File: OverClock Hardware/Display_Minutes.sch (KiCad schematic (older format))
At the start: 40 parts, among them U3 10M02SCE144

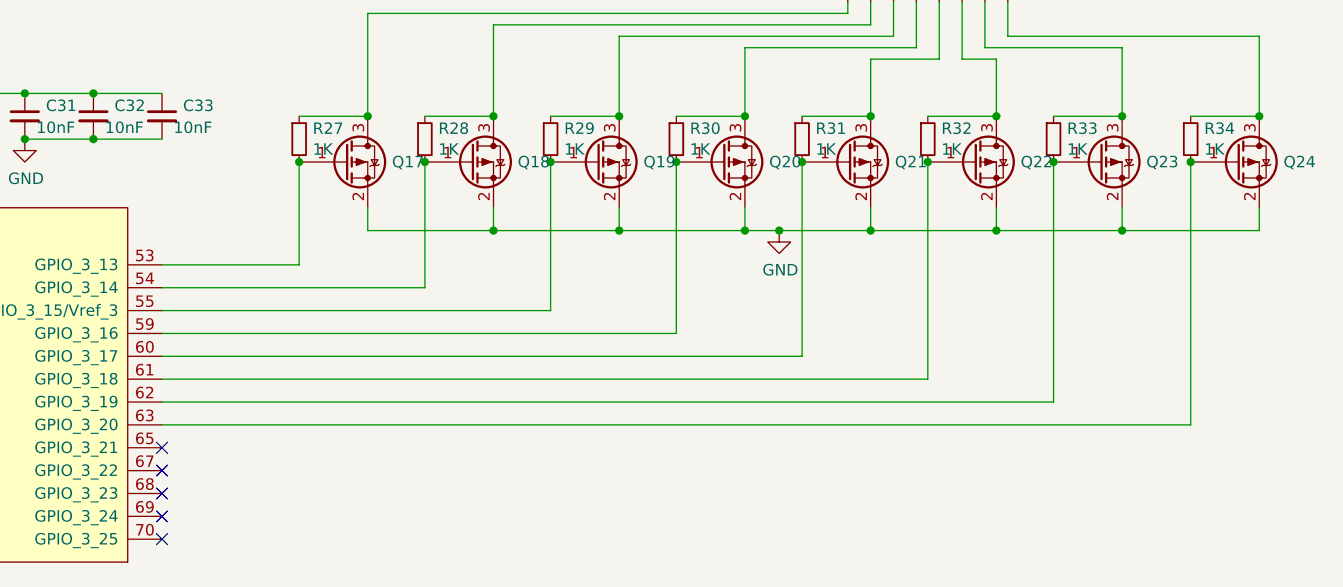
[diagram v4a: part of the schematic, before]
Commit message: Rerouted 7 Segment Displays
Rearranged the displays for cleaner routing, also modified the schematic for some of the displays to allow for better routing.
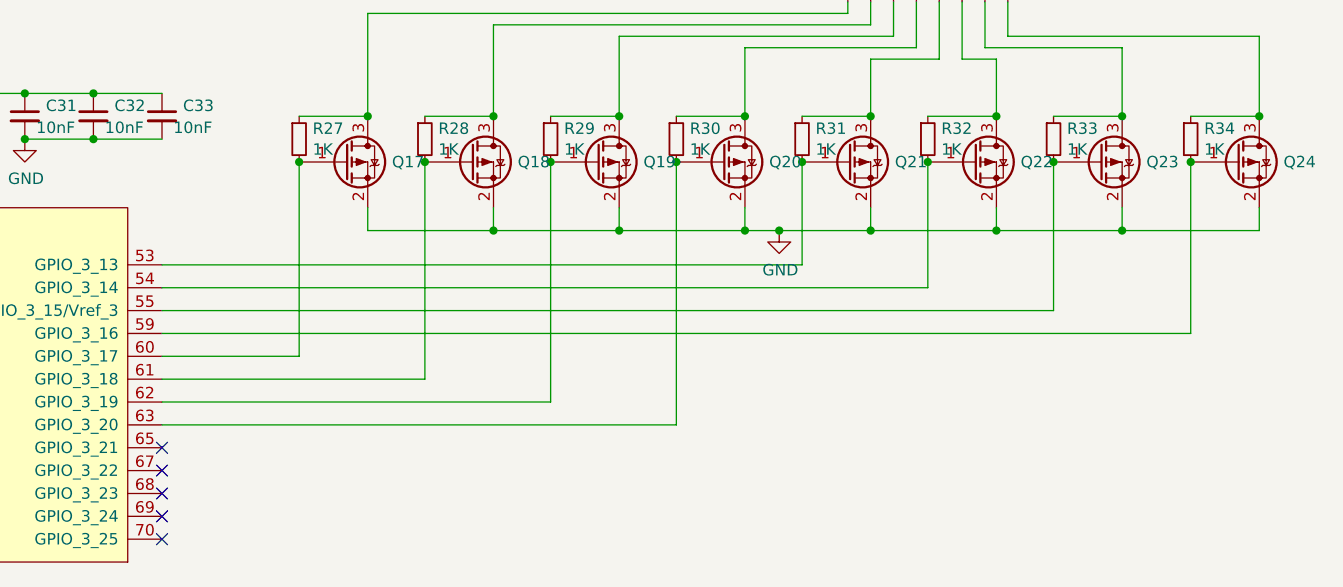
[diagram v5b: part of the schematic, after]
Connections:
- net at Q18.1 (G), R28.2: now also U3.61 (GPIO_3_18); no longer U3.54 (GPIO_3_14)
- net at Q17.1 (G), R27.2: now also U3.60 (GPIO_3_17); no longer U3.53 (GPIO_3_13)
- net at Q19.1 (G), R29.2: now also U3.62 (GPIO_3_19); no longer U3.55 (GPIO_3_15/Vref_3)
- net at Q20.1 (G), R30.2: now also U3.63 (GPIO_3_20); no longer U3.59 (GPIO_3_16)
- net at Q21.1 (G), R31.2: now also U3.53 (GPIO_3_13); no longer U3.60 (GPIO_3_17)
- net at Q22.1 (G), R32.2: now also U3.54 (GPIO_3_14); no longer U3.61 (GPIO_3_18)
- net at Q23.1 (G), R33.2: now also U3.55 (GPIO_3_15/Vref_3); no longer U3.62 (GPIO_3_19)
- net at Q24.1 (G), R34.2: now also U3.59 (GPIO_3_16); no longer U3.63 (GPIO_3_20)
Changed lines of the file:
@@
 	14300 4350 14600 4350
 Wire Wire Line
-	10400 4550 10400 5000
-Wire Wire Line
-	10400 5000 9800 5000
-Connection ~ 10400 4550
-Wire Wire Line
-	10950 4550 10950 5100
-Wire Wire Line
-	10950 5100 9800 5100
-Wire Wire Line
-	11500 4550 11500 5200
-Wire Wire Line
-	11500 5200 9800 5200
-Wire Wire Line
-	12050 4550 12050 5300
-Wire Wire Line
-	12050 5300 9800 5300
-Wire Wire Line
-	12600 4550 12600 5400
-Wire Wire Line
-	12600 5400 9800 5400
-Wire Wire Line
-	13150 4550 13150 5500
-Wire Wire Line
-	13150 5500 9800 5500
-Wire Wire Line
-	13700 4550 13700 5600
-Wire Wire Line
-	13700 5600 9800 5600
-Wire Wire Line
-	14300 4550 14300 5700
-Wire Wire Line
-	14300 5700 9800 5700
+	12600 4550 12600 5000
+Wire Wire Line
+	13700 4550 13700 5200
+Wire Wire Line
+	14300 4550 14300 5300
 Wire Wire Line
 	14600 4000 14600 4350
@@
 	1    0    0    -1
 $EndComp
-Connection ~ 10950 4550
 Connection ~ 11250 4350
 $Comp
@@
 	1    0    0    -1
 $EndComp
-Connection ~ 11500 4550
 Connection ~ 11800 4350
-Connection ~ 12050 4550
 Connection ~ 12350 4350
 Connection ~ 12600 4550
@@
 Connection ~ 7300 4400
 Connection ~ 7900 4400
+Wire Wire Line
+	7600 4600 7600 5050
+Wire Wire Line
+	7600 5050 8150 5050
+Connection ~ 7600 4600
+Wire Wire Line
+	7000 4600 7000 5150
+Wire Wire Line
+	7000 5150 8150 5150
+Connection ~ 7000 4600
+Wire Wire Line
+	6450 4600 6450 5250
+Wire Wire Line
+	6450 5250 8150 5250
+Connection ~ 6450 4600
+Wire Wire Line
+	5900 4600 5900 5350
+Wire Wire Line
+	5900 5350 8150 5350
+Connection ~ 5900 4600
+Wire Wire Line
+	5350 4600 5350 5450
+Wire Wire Line
+	5350 5450 8150 5450
+Connection ~ 5350 4600
+Wire Wire Line
+	4800 4600 4800 5550
+Wire Wire Line
+	4800 5550 8150 5550
+Connection ~ 4800 4600
+Wire Wire Line
+	4250 4600 4250 5650
+Wire Wire Line
+	4250 5650 8150 5650
+Connection ~ 4250 4600
+Wire Wire Line
+	3700 4600 3700 5750
+Wire Wire Line
+	3700 5750 8150 5750
+Connection ~ 3700 4600
+Text GLabel 8600 4250 0    50   Input ~ 0
++3V
+$Comp
+L power:GND #PWR021
+U 1 1 5CBB2B7C
+P 9200 4450
+F 0 "#PWR021" H 9200 4200 50  0001 C CNN
+F 1 "GND" H 9205 4277 50  0000 C CNN
+F 2 "" H 9200 4450 50  0001 C CNN
+F 3 "" H 9200 4450 50  0001 C CNN
+	1    9200 4450
+	1    0    0    -1
+$EndComp
+Wire Wire Line
+	8600 4250 8850 4250
+Connection ~ 8850 4250
+Wire Wire Line
+	8850 4250 8850 4600
+Connection ~ 9200 4450
+Wire Wire Line
+	9200 4250 8850 4250
+Connection ~ 9200 4250
+$Comp
+L Device:C_Small C31
+U 1 1 5CB98270
+P 9200 4350
+F 0 "C31" H 9292 4396 50  0000 L CNN
+F 1 "10nF" H 9250 4300 50  0000 L CNN
+F 2 "Capacitor_SMD:C_0603_1608Metric_Pad1.05x0.95mm_HandSolder" H 9200 4350 50  0001 C CNN
+F 3 "~" H 9200 4350 50  0001 C CNN
+	1    9200 4350
+	1    0    0    -1
+$EndComp
+$Comp
+L Device:C_Small C33
+U 1 1 5CB8F8E1
+P 9800 4350
+F 0 "C33" H 9892 4396 50  0000 L CNN
+F 1 "10nF" H 9850 4300 50  0000 L CNN
+F 2 "Capacitor_SMD:C_0603_1608Metric_Pad1.05x0.95mm_HandSolder" H 9800 4350 50  0001 C CNN
+F 3 "~" H 9800 4350 50  0001 C CNN
+	1    9800 4350
+	1    0    0    -1
+$EndComp
+Wire Wire Line
+	9500 4450 9200 4450
+Wire Wire Line
+	9800 4450 9500 4450
+Connection ~ 9500 4450
+Wire Wire Line
+	9500 4250 9200 4250
+Wire Wire Line
+	9800 4250 9500 4250
+Connection ~ 9500 4250
+$Comp
+L Device:C_Small C32
+U 1 1 5CB8F75B
+P 9500 4350
+F 0 "C32" H 9592 4396 50  0000 L CNN
+F 1 "10nF" H 9550 4300 50  0000 L CNN
+F 2 "Capacitor_SMD:C_0603_1608Metric_Pad1.05x0.95mm_HandSolder" H 9500 4350 50  0001 C CNN
+F 3 "~" H 9500 4350 50  0001 C CNN
+	1    9500 4350
+	1    0    0    -1
+$EndComp
+NoConn ~ 9800 6200
+NoConn ~ 9800 6100
+NoConn ~ 9800 6000
+NoConn ~ 9800 5900
+NoConn ~ 9800 5800
+NoConn ~ 8150 6150
+NoConn ~ 8150 6050
+NoConn ~ 8150 5950
+NoConn ~ 8150 5850
+Connection ~ 8850 4600
+Wire Wire Line
+	8950 4600 8850 4600
+Wire Wire Line
+	9050 4600 8950 4600
+Connection ~ 8950 4600
 $Comp
 L Maxted_Libs:10M02SCE144 U3
@@
 $EndComp
 Wire Wire Line
-	7600 4600 7600 5050
-Wire Wire Line
-	7600 5050 8150 5050
-Connection ~ 7600 4600
-Wire Wire Line
-	7000 4600 7000 5150
-Wire Wire Line
-	7000 5150 8150 5150
-Connection ~ 7000 4600
-Wire Wire Line
-	6450 4600 6450 5250
-Wire Wire Line
-	6450 5250 8150 5250
-Connection ~ 6450 4600
-Wire Wire Line
-	5900 4600 5900 5350
-Wire Wire Line
-	5900 5350 8150 5350
-Connection ~ 5900 4600
-Wire Wire Line
-	5350 4600 5350 5450
-Wire Wire Line
-	5350 5450 8150 5450
-Connection ~ 5350 4600
-Wire Wire Line
-	4800 4600 4800 5550
-Wire Wire Line
-	4800 5550 8150 5550
-Connection ~ 4800 4600
-Wire Wire Line
-	4250 4600 4250 5650
-Wire Wire Line
-	4250 5650 8150 5650
-Connection ~ 4250 4600
-Wire Wire Line
-	3700 4600 3700 5750
-Wire Wire Line
-	3700 5750 8150 5750
-Connection ~ 3700 4600
-NoConn ~ 8150 5850
-NoConn ~ 8150 5950
-NoConn ~ 8150 6050
-NoConn ~ 8150 6150
-NoConn ~ 9800 5800
-NoConn ~ 9800 5900
-NoConn ~ 9800 6000
-NoConn ~ 9800 6100
-NoConn ~ 9800 6200
-Wire Wire Line
-	9050 4600 8950 4600
-Connection ~ 8950 4600
-Wire Wire Line
-	8950 4600 8850 4600
-$Comp
-L Device:C_Small C32
-U 1 1 5CB8F75B
-P 9500 4350
-F 0 "C32" H 9592 4396 50  0000 L CNN
-F 1 "10nF" H 9550 4300 50  0000 L CNN
-F 2 "Capacitor_SMD:C_0603_1608Metric_Pad1.05x0.95mm_HandSolder" H 9500 4350 50  0001 C CNN
-F 3 "~" H 9500 4350 50  0001 C CNN
-	1    9500 4350
-	1    0    0    -1
-$EndComp
-$Comp
-L Device:C_Small C33
-U 1 1 5CB8F8E1
-P 9800 4350
-F 0 "C33" H 9892 4396 50  0000 L CNN
-F 1 "10nF" H 9850 4300 50  0000 L CNN
-F 2 "Capacitor_SMD:C_0603_1608Metric_Pad1.05x0.95mm_HandSolder" H 9800 4350 50  0001 C CNN
-F 3 "~" H 9800 4350 50  0001 C CNN
-	1    9800 4350
-	1    0    0    -1
-$EndComp
-$Comp
-L Device:C_Small C31
-U 1 1 5CB98270
-P 9200 4350
-F 0 "C31" H 9292 4396 50  0000 L CNN
-F 1 "10nF" H 9250 4300 50  0000 L CNN
-F 2 "Capacitor_SMD:C_0603_1608Metric_Pad1.05x0.95mm_HandSolder" H 9200 4350 50  0001 C CNN
-F 3 "~" H 9200 4350 50  0001 C CNN
-	1    9200 4350
-	1    0    0    -1
-$EndComp
-Wire Wire Line
-	9800 4250 9500 4250
-Wire Wire Line
-	8850 4250 8850 4600
-Connection ~ 9200 4250
-Wire Wire Line
-	9200 4250 8850 4250
-Connection ~ 9500 4250
-Wire Wire Line
-	9500 4250 9200 4250
-Connection ~ 8850 4600
-Wire Wire Line
-	9800 4450 9500 4450
-Connection ~ 9500 4450
-Wire Wire Line
-	9500 4450 9200 4450
-$Comp
-L power:GND #PWR021
-U 1 1 5CBB2B7C
-P 9200 4450
-F 0 "#PWR021" H 9200 4200 50  0001 C CNN
-F 1 "GND" H 9205 4277 50  0000 C CNN
-F 2 "" H 9200 4450 50  0001 C CNN
-F 3 "" H 9200 4450 50  0001 C CNN
-	1    9200 4450
-	1    0    0    -1
-$EndComp
-Connection ~ 9200 4450
-Text GLabel 8600 4250 0    50   Input ~ 0
-+3V
-Wire Wire Line
-	8600 4250 8850 4250
-Connection ~ 8850 4250
+	9800 5000 12600 5000
+Wire Wire Line
+	9800 5100 13150 5100
+Wire Wire Line
+	13150 4550 13150 5100
+Wire Wire Line
+	9800 5200 13700 5200
+Wire Wire Line
+	9800 5300 14300 5300
+Wire Wire Line
+	12050 4550 12050 5700
+Wire Wire Line
+	12050 5700 9800 5700
+Connection ~ 12050 4550
+Wire Wire Line
+	11500 4550 11500 5600
+Wire Wire Line
+	11500 5600 9800 5600
+Connection ~ 11500 4550
+Wire Wire Line
+	10950 4550 10950 5500
+Wire Wire Line
+	10950 5500 9800 5500
+Connection ~ 10950 4550
+Wire Wire Line
+	10400 4550 10400 5400
+Wire Wire Line
+	10400 5400 9800 5400
+Connection ~ 10400 4550
 $EndSCHEMATC
